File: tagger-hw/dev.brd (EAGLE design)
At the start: 65.7 x 62.2 mm, 50 parts, among them J2 22-23-2021, J3 22-23-2021, X1 EXC-31B

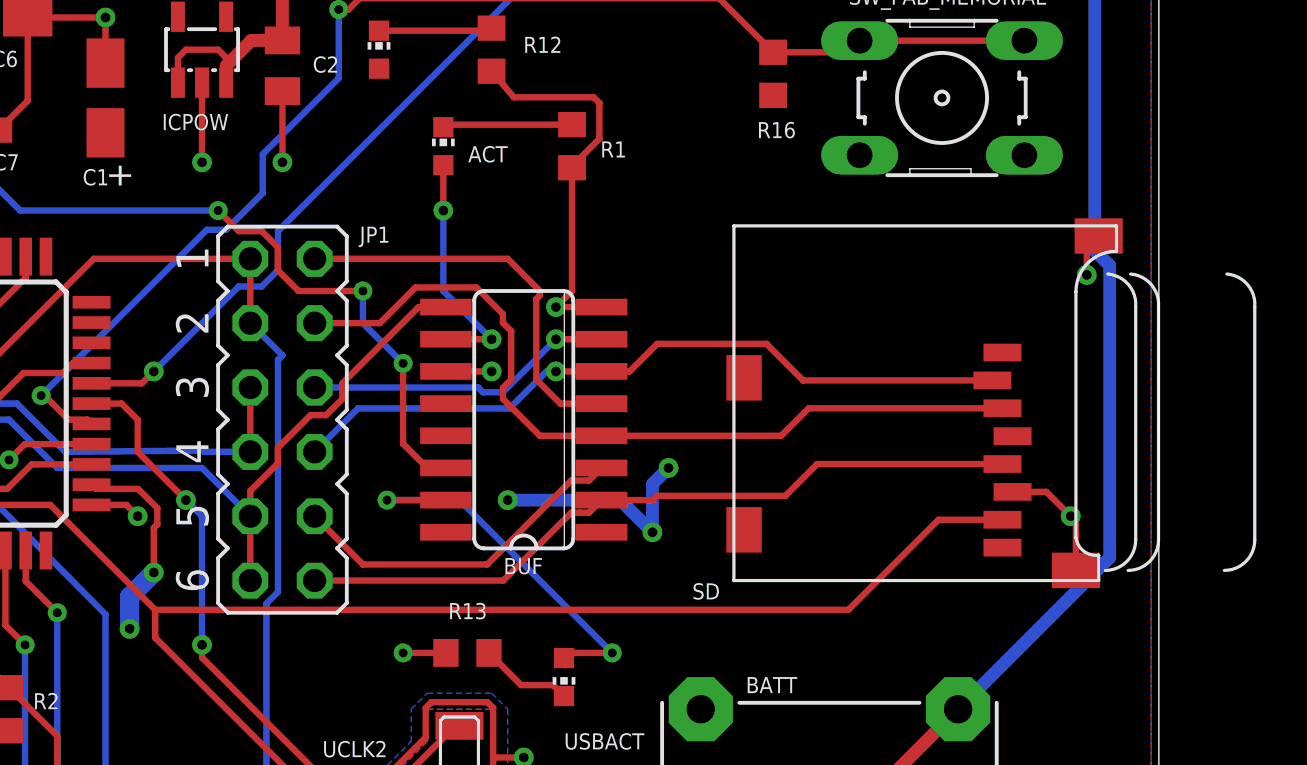
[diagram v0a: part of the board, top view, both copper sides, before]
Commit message: New microSD slot pattern
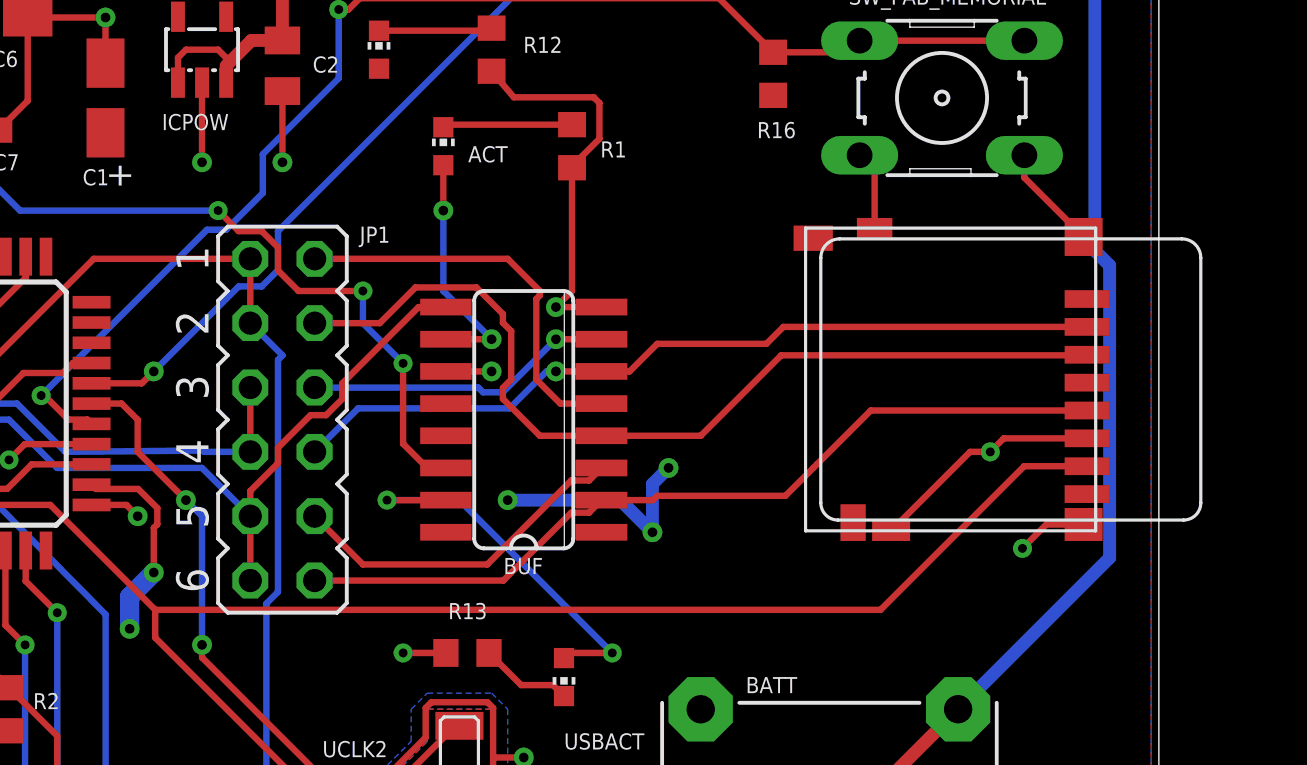
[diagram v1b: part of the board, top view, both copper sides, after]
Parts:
- removed SD: MICROSD, adafruit:MICROSD
- added U$1: MICROSD, dorskyee:MICROSD
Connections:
- net +3V3: now also U$1.VDD; no longer SD.4
- net CS_OUT: now also U$1.CS; no longer SD.2
- net GND: now also U$1.MNT@1, U$1.MNT@2, U$1.MNT@3, U$1.MNT@4, U$1.VSS; no longer SD.6, SD.MT1, SD.MT2
- net MISO: now also U$1.MISO; no longer SD.7
- net MOSI_OUT: now also U$1.MOSI; no longer SD.3
- net SCK_OUT: now also U$1.SCK; no longer SD.5
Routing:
- net GND: track 115.9 -> 128.6 mm
- net SCK_OUT: track 29.1 -> 33.3 mm
- net MOSI_OUT: track 32.8 -> 37.0 mm
- net MISO: track 71.8 -> 76.0 mm
- net CS_OUT: track 29.1 -> 32.5 mm
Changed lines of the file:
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@@
 <setting verticaltext="up"/>
 </settings>
-<grid distance="12.5" unitdist="mil" unit="mil" style="lines" multiple="1" display="no" altdistance="5" altunitdist="mil" altunit="mil"/>
+<grid distance="25" unitdist="mil" unit="mil" style="lines" multiple="2" display="no" altdistance="5" altunitdist="mil" altunit="mil"/>
 <layers>
 <layer number="1" name="Top" color="4" fill="1" visible="yes" active="yes"/>
@@
 <attribute name="VALUE" x="44.831" y="47.498" size="0.635" layer="27" font="vector" rot="R90"/>
 </element>
-<element name="SD" library="adafruit" package="MICROSD" value="MICROSD" x="48.895" y="31.115" smashed="yes" rot="R90">
-<attribute name="NAME" x="48.39" y="31.005" size="0.635" layer="25" font="vector" rot="R180"/>
-</element>
 <element name="BUF" library="40xx" library_urn="urn:adsk.eagle:library:80" package="SO16" package3d_urn="urn:adsk.eagle:package:821/2" value="4010D" x="40.64" y="37.465" smashed="yes" rot="R90">
 <attribute name="NAME" x="41.402" y="32.004" size="0.635" layer="25" font="vector" ratio="10" rot="R180"/>
@@
 <attribute name="VALUE" x="48.5775" y="51.7525" size="1.27" layer="27" rot="R270"/>
 </element>
+<element name="U$1" library="dorskyee" package="MICROSD" value="MICROSD" x="62.865" y="42.2275" rot="R90"/>
 </elements>
 <signals>
@@
 <wire x1="44.45" y1="34.29" x2="45.72" y2="33.02" width="0.508" layer="16"/>
 <via x="45.72" y="33.02" extent="1-16" drill="0.381"/>
-<contactref element="SD" pad="4"/>
 <wire x1="45.72" y1="33.02" x2="45.72" y2="34.925" width="0.508" layer="16"/>
 <wire x1="45.72" y1="34.925" x2="46.355" y2="35.56" width="0.508" layer="16"/>
@@
 <contactref element="R15" pad="2"/>
 <contactref element="R16" pad="2"/>
+<contactref element="U$1" pad="VDD"/>
 </signal>
 <signal name="GND">
@@
 <wire x1="21.06" y1="53.34" x2="21.06" y2="50.055" width="0.254" layer="1"/>
 <wire x1="21.06" y1="50.055" x2="19.9" y2="48.895" width="0.254" layer="1"/>
-<contactref element="SD" pad="6"/>
-<contactref element="SD" pad="MT2"/>
-<contactref element="SD" pad="MT1"/>
-<wire x1="62.435" y1="31.515" x2="62.435" y2="33.45" width="0.254" layer="1"/>
-<wire x1="62.435" y1="33.45" x2="62.23" y2="33.655" width="0.254" layer="1"/>
-<via x="62.23" y="33.655" extent="1-16" drill="0.381"/>
-<wire x1="62.23" y1="33.655" x2="61.27" y2="34.615" width="0.254" layer="1"/>
-<wire x1="61.27" y1="34.615" x2="59.935" y2="34.615" width="0.254" layer="1"/>
-<wire x1="63.335" y1="44.715" x2="62.865" y2="44.245" width="0.254" layer="1"/>
-<wire x1="62.865" y1="44.245" x2="62.865" y2="43.18" width="0.254" layer="1"/>
-<via x="62.865" y="43.18" extent="1-16" drill="0.381"/>
 <contactref element="UCLK2" pad="P$4"/>
 <contactref element="C9" pad="2"/>
@@
 <contactref element="SW_FAB_MEMORIAL" pad="4"/>
 <contactref element="SW_FAB_MEMORIAL" pad="3"/>
+<contactref element="U$1" pad="VSS"/>
+<wire x1="62.865" y1="36.7275" x2="59.5875" y2="36.7275" width="0.254" layer="1"/>
+<wire x1="59.5875" y1="36.7275" x2="59.055" y2="36.195" width="0.254" layer="1"/>
+<via x="59.055" y="36.195" extent="1-16" drill="0.35"/>
+<contactref element="U$1" pad="MNT@4"/>
+<contactref element="U$1" pad="MNT@3"/>
+<contactref element="U$1" pad="MNT@2"/>
+<contactref element="U$1" pad="MNT@1"/>
+<wire x1="55.14" y1="33.0775" x2="58.2575" y2="36.195" width="0.254" layer="1"/>
+<wire x1="58.2575" y1="36.195" x2="59.055" y2="36.195" width="0.254" layer="1"/>
+<wire x1="62.74" y1="44.6775" x2="60.4012" y2="47.0163" width="0.254" layer="1"/>
+<wire x1="60.4012" y1="47.0163" x2="60.4012" y2="47.9044" width="0.254" layer="1"/>
+<wire x1="54.49" y1="45.0275" x2="54.49" y2="47.3132" width="0.254" layer="1"/>
+<wire x1="54.49" y1="47.3132" x2="53.8988" y2="47.9044" width="0.254" layer="1"/>
+<wire x1="62.74" y1="33.3275" x2="61.2675" y2="33.3275" width="0.254" layer="1"/>
+<wire x1="61.2675" y1="33.3275" x2="60.325" y2="32.385" width="0.254" layer="1"/>
+<via x="60.325" y="32.385" extent="1-16" drill="0.35"/>
 </signal>
 <signal name="VCC">
@@
 </signal>
 <signal name="MISO">
-<contactref element="SD" pad="7"/>
 <contactref element="UC" pad="11"/>
 <contactref element="ISP1" pad="1"/>
 <wire x1="11.98" y1="34.1" x2="21.95138125" y2="34.1" width="0.254" layer="1"/>
-<wire x1="53.4543" y1="29.9593" x2="57.01" y2="33.515" width="0.254" layer="1"/>
-<wire x1="59.535" y1="33.515" x2="57.01" y2="33.515" width="0.254" layer="1"/>
 <wire x1="10.85809375" y1="34.1" x2="11.98" y2="34.1" width="0.254" layer="1"/>
 <wire x1="8.14079375" y1="36.8173" x2="10.85809375" y2="34.1" width="0.254" layer="1"/>
@@
 <wire x1="7.12460625" y1="36.8173" x2="8.14079375" y2="36.8173" width="0.254" layer="1"/>
 <wire x1="6.3627" y1="37.57920625" x2="7.12460625" y2="36.8173" width="0.254" layer="1"/>
-<wire x1="26.09208125" y1="29.9593" x2="53.4543" y2="29.9593" width="0.254" layer="1"/>
+<wire x1="26.09208125" y1="29.9593" x2="54.7243" y2="29.9593" width="0.254" layer="1"/>
 <wire x1="21.95138125" y1="34.1" x2="26.09208125" y2="29.9593" width="0.254" layer="1"/>
 <contactref element="UCLK2" pad="P$2"/>
@@
 <wire x1="32.3071875" y1="22.644" x2="26.09208125" y2="28.85910625" width="0.254" layer="1"/>
 <wire x1="26.09208125" y1="28.85910625" x2="26.09208125" y2="29.9593" width="0.254" layer="1"/>
+<contactref element="U$1" pad="MISO"/>
+<wire x1="60.3925" y1="35.6275" x2="62.865" y2="35.6275" width="0.254" layer="1"/>
+<wire x1="54.7243" y1="29.9593" x2="60.3925" y2="35.6275" width="0.254" layer="1"/>
 </signal>
 <signal name="SD_ACT_D">
@@
 </signal>
 <signal name="MOSI_OUT">
-<contactref element="SD" pad="3"/>
 <contactref element="JP1" pad="4"/>
 <contactref element="BUF" pad="4"/>
-<wire x1="51.885" y1="37.915" x2="59.535" y2="37.915" width="0.254" layer="1"/>
-<wire x1="43.7134" y1="36.83" x2="50.8" y2="36.83" width="0.254" layer="1"/>
-<wire x1="50.8" y1="36.83" x2="51.885" y2="37.915" width="0.254" layer="1"/>
 <wire x1="36.36648125" y1="42.6847" x2="38.76671875" y2="42.6847" width="0.254" layer="1"/>
 <wire x1="32.385" y1="41.275" x2="34.95678125" y2="41.275" width="0.254" layer="1"/>
@@
 <wire x1="39.8173" y1="38.72170625" x2="39.8173" y2="38.2877" width="0.254" layer="1"/>
 <wire x1="40.1447" y1="40.96089375" x2="40.1447" y2="39.04910625" width="0.254" layer="1"/>
+<contactref element="U$1" pad="MOSI"/>
+<wire x1="62.865" y1="40.0275" x2="62.8425" y2="40.005" width="0.254" layer="1"/>
+<wire x1="62.8425" y1="40.005" x2="50.8" y2="40.005" width="0.254" layer="1"/>
+<wire x1="47.625" y1="36.83" x2="43.7134" y2="36.83" width="0.254" layer="1"/>
+<wire x1="50.8" y1="40.005" x2="47.625" y2="36.83" width="0.254" layer="1"/>
 </signal>
 <signal name="SCK_OUT">
-<contactref element="SD" pad="5"/>
 <contactref element="BUF" pad="2"/>
 <wire x1="43.7134" y1="34.29" x2="45.74138125" y2="34.29" width="0.254" layer="1"/>
-<wire x1="59.535" y1="35.715" x2="52.225" y2="35.715" width="0.254" layer="1"/>
-<wire x1="50.9695" y1="34.4595" x2="52.225" y2="35.715" width="0.254" layer="1"/>
+<wire x1="50.9695" y1="34.4595" x2="52.07" y2="35.56" width="0.254" layer="1"/>
 <contactref element="JP1" pad="12"/>
+<wire x1="52.07" y1="35.56" x2="52.225" y2="35.715" width="0.254" layer="1"/>
 <wire x1="43.7134" y1="34.29" x2="43.2181" y2="33.7947" width="0.254" layer="1"/>
-<wire x1="43.2181" y1="33.7947" x2="42.8625" y2="33.7947" width="0.254" layer="1"/>
-<wire x1="42.8625" y1="33.7947" x2="42.51328125" y2="33.7947" width="0.254" layer="1"/>
+<wire x1="43.2181" y1="33.7947" x2="42.51328125" y2="33.7947" width="0.254" layer="1"/>
 <wire x1="39.83358125" y1="31.115" x2="32.385" y2="31.115" width="0.254" layer="1"/>
 <wire x1="42.51328125" y1="33.7947" x2="39.83358125" y2="31.115" width="0.254" layer="1"/>
 <wire x1="45.74138125" y1="34.29" x2="45.91088125" y2="34.4595" width="0.254" layer="1"/>
 <wire x1="45.91088125" y1="34.4595" x2="50.9695" y2="34.4595" width="0.254" layer="1"/>
+<contactref element="U$1" pad="SCK"/>
+<wire x1="62.865" y1="37.8275" x2="54.3375" y2="37.8275" width="0.254" layer="1"/>
+<wire x1="54.3375" y1="37.8275" x2="52.225" y2="35.715" width="0.254" layer="1"/>
 </signal>
 <signal name="CS_OUT">
-<contactref element="SD" pad="2"/>
 <contactref element="BUF" pad="6"/>
 <wire x1="43.7134" y1="39.37" x2="44.82138125" y2="39.37" width="0.254" layer="1"/>
-<wire x1="51.66361875" y1="39.015" x2="50.21911875" y2="40.4595" width="0.254" layer="1"/>
-<wire x1="59.135" y1="39.015" x2="51.66361875" y2="39.015" width="0.254" layer="1"/>
 <contactref element="JP1" pad="8"/>
 <wire x1="43.7134" y1="39.37" x2="41.91" y2="39.37" width="0.254" layer="1"/>
@@
 <wire x1="44.82138125" y1="39.37" x2="45.91088125" y2="40.4595" width="0.254" layer="1"/>
 <wire x1="45.91088125" y1="40.4595" x2="50.21911875" y2="40.4595" width="0.254" layer="1"/>
+<contactref element="U$1" pad="CS"/>
+<wire x1="62.865" y1="41.1275" x2="50.88711875" y2="41.1275" width="0.254" layer="1"/>
+<wire x1="50.88711875" y1="41.1275" x2="50.21911875" y2="40.4595" width="0.254" layer="1"/>
 </signal>
 <signal name="VBAT">

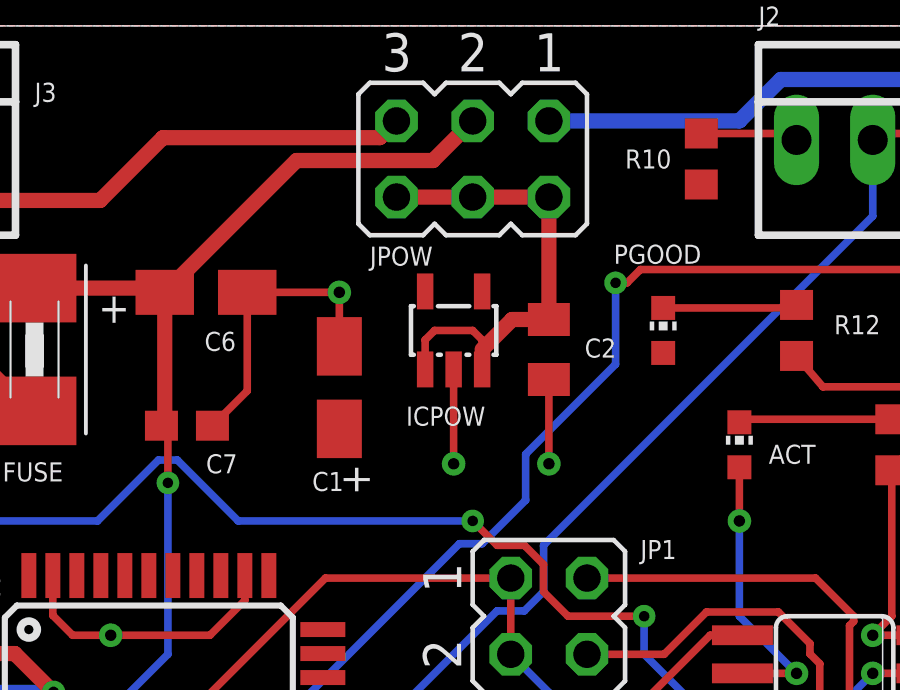
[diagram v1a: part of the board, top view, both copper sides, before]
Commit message: Add current sense resistor, calculations
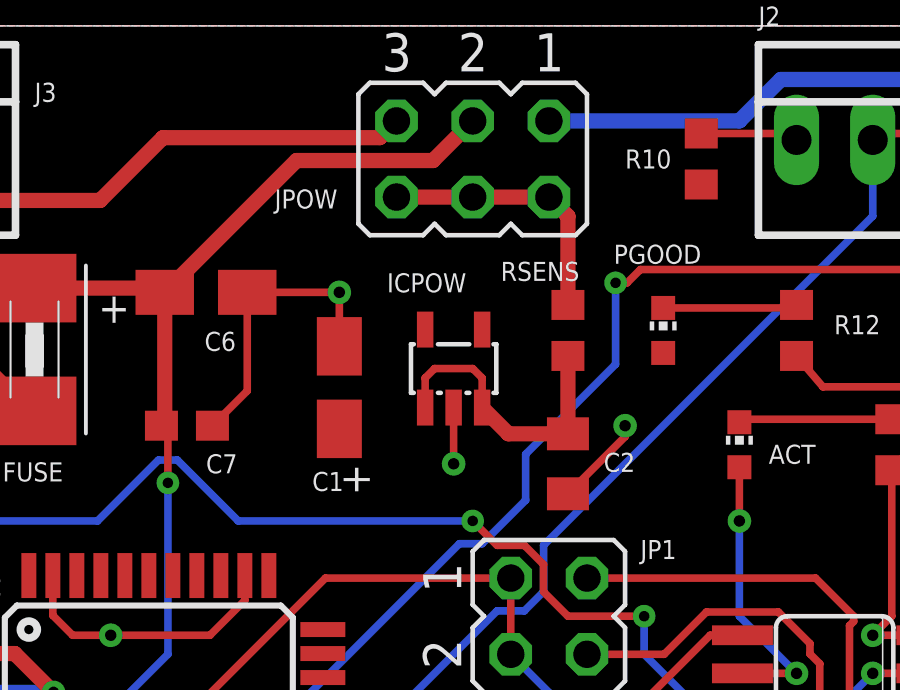
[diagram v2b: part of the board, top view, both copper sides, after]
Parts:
- added RSENS: 1R, adafruit:R0603
- moved C2 3.86 mm to (31.8, 47.6)
- moved ICPOW 1.27 mm to (27.9, 50.8)
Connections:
- new net VCC_R: C2.1, ICPOW.1, ICPOW.3, RSENS.1
- net VCC: now also RSENS.2; no longer C2.1, ICPOW.1, ICPOW.3
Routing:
- net VCC_R: track 0.00 -> 9.95 mm
- net VCC: track 15.9 -> 8.94 mm
- net GND: track 128.6 -> 127.6 mm
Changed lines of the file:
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@@
 <attribute name="VALUE" x="21.805" y="52.115" size="0.635" layer="27" font="vector" rot="R270"/>
 </element>
-<element name="C2" library="adafruit" package="C0805K" value="0.1uF" x="31.115" y="51.435" smashed="yes" rot="R270">
-<attribute name="NAME" x="32.3075" y="51.165" size="0.635" layer="25" font="vector"/>
-<attribute name="VALUE" x="29.215" y="52.435" size="0.635" layer="27" font="vector" rot="R270"/>
-</element>
-<element name="ICPOW" library="adafruit" package="SOT23-5L" value="CAT6219-330TDGT3" x="27.94" y="52.07" smashed="yes">
-<attribute name="NAME" x="26.3525" y="48.895" size="0.635" layer="25" font="vector"/>
-<attribute name="VALUE" x="26.035" y="48.641" size="0.635" layer="27" font="vector"/>
+<element name="C2" library="adafruit" package="C0805K" value="0.1uF" x="31.75" y="47.625" smashed="yes" rot="R270">
+<attribute name="NAME" x="32.9425" y="47.355" size="0.635" layer="25" font="vector"/>
+<attribute name="VALUE" x="29.85" y="48.625" size="0.635" layer="27" font="vector" rot="R270"/>
+</element>
+<element name="ICPOW" library="adafruit" package="SOT23-5L" value="CAT6219-330TDGT3" x="27.94" y="50.8" smashed="yes">
+<attribute name="NAME" x="25.7175" y="53.34" size="0.635" layer="25" font="vector"/>
+<attribute name="VALUE" x="26.035" y="47.371" size="0.635" layer="27" font="vector"/>
 </element>
 <element name="R1" library="adafruit" package="R0603" value="1K" x="42.545" y="48.26" smashed="yes" rot="R90">
@@
 </element>
 <element name="JPOW" library="jumper" library_urn="urn:adsk.eagle:library:252" package="JP3Q" package3d_urn="urn:adsk.eagle:package:15460/1" value="HDR100IMP40M-G-V-TH" x="28.575" y="57.785" smashed="yes" rot="R180">
-<attribute name="NAME" x="27.2415" y="54.864" size="0.635" layer="25" font="vector" ratio="10" rot="R180"/>
+<attribute name="NAME" x="24.0665" y="56.769" size="0.635" layer="25" font="vector" ratio="10" rot="R180"/>
 <attribute name="VALUE" x="32.004" y="63.627" size="0.635" layer="27" font="vector" ratio="10" rot="R180"/>
 </element>
@@
 </element>
 <element name="U$1" library="dorskyee" package="MICROSD" value="MICROSD" x="62.865" y="42.2275" rot="R90"/>
+<element name="RSENS" library="adafruit" package="R0603" value="1R" x="31.75" y="52.07" smashed="yes" rot="R90">
+<attribute name="NAME" x="32.131" y="54.356" size="0.635" layer="25" font="vector" rot="R180"/>
+<attribute name="VALUE" x="33.782" y="51.181" size="1.27" layer="27" rot="R90"/>
+</element>
 </elements>
 <signals>
@@
 <wire x1="24.955" y1="34.1" x2="25.4" y2="33.655" width="0.254" layer="1"/>
 <via x="25.4" y="33.655" extent="1-16" drill="0.381"/>
-<wire x1="27.94" y1="50.77" x2="27.94" y2="47.625" width="0.254" layer="1"/>
+<wire x1="27.94" y1="49.5" x2="27.94" y2="47.625" width="0.254" layer="1"/>
 <via x="27.94" y="47.625" extent="1-16" drill="0.381"/>
 <wire x1="24.13" y1="51.54" x2="24.13" y2="53.34" width="0.254" layer="1"/>
 <via x="24.13" y="53.34" extent="1-16" drill="0.381"/>
-<wire x1="31.115" y1="50.435" x2="31.115" y2="47.625" width="0.254" layer="1"/>
-<via x="31.115" y="47.625" extent="1-16" drill="0.381"/>
+<via x="33.655" y="48.895" extent="1-16" drill="0.381"/>
 <wire x1="29.77" y1="8.89" x2="31.75" y2="8.89" width="0.254" layer="1"/>
 <via x="31.75" y="8.89" extent="1-16" drill="0.381"/>
@@
 <wire x1="61.2675" y1="33.3275" x2="60.325" y2="32.385" width="0.254" layer="1"/>
 <via x="60.325" y="32.385" extent="1-16" drill="0.35"/>
+<wire x1="31.75" y1="46.625" x2="33.655" y2="48.53" width="0.254" layer="1"/>
+<wire x1="33.655" y1="48.53" x2="33.655" y2="48.895" width="0.254" layer="1"/>
 </signal>
 <signal name="VCC">
-<contactref element="ICPOW" pad="1"/>
-<contactref element="C2" pad="1"/>
-<contactref element="ICPOW" pad="3"/>
 <contactref element="JPOW" pad="2"/>
 <contactref element="JPOW" pad="6"/>
@@
 <wire x1="26.035" y1="56.515" x2="28.575" y2="56.515" width="0.508" layer="1"/>
 <wire x1="28.575" y1="56.515" x2="31.115" y2="56.515" width="0.508" layer="1"/>
-<wire x1="31.115" y1="52.435" x2="31.115" y2="56.515" width="0.508" layer="1"/>
-<wire x1="26.99" y1="50.77" x2="26.99" y2="51.755" width="0.254" layer="1"/>
-<wire x1="26.99" y1="51.755" x2="27.305" y2="52.07" width="0.254" layer="1"/>
-<wire x1="27.305" y1="52.07" x2="28.575" y2="52.07" width="0.254" layer="1"/>
-<wire x1="28.89" y1="51.755" x2="28.575" y2="52.07" width="0.254" layer="1"/>
-<wire x1="28.89" y1="50.77" x2="28.89" y2="51.435" width="0.254" layer="1"/>
-<wire x1="28.89" y1="51.435" x2="28.89" y2="51.755" width="0.254" layer="1"/>
-<wire x1="31.115" y1="52.435" x2="29.89" y2="52.435" width="0.508" layer="1"/>
-<wire x1="29.89" y1="52.435" x2="28.89" y2="51.435" width="0.508" layer="1"/>
+<wire x1="31.115" y1="56.515" x2="31.75" y2="55.88" width="0.508" layer="1"/>
+<contactref element="RSENS" pad="2"/>
+<wire x1="31.75" y1="55.88" x2="31.75" y2="52.92" width="0.508" layer="1"/>
 </signal>
 <signal name="MISO">
@@
 <wire x1="26.3236875" y1="5.6125" x2="29.21" y2="5.6125" width="0.254" layer="1"/>
 </signal>
+<signal name="VCC_R">
+<contactref element="ICPOW" pad="1"/>
+<contactref element="ICPOW" pad="3"/>
+<wire x1="26.99" y1="49.5" x2="26.99" y2="50.485" width="0.254" layer="1"/>
+<wire x1="26.99" y1="50.485" x2="27.305" y2="50.8" width="0.254" layer="1"/>
+<wire x1="27.305" y1="50.8" x2="28.575" y2="50.8" width="0.254" layer="1"/>
+<wire x1="28.89" y1="50.485" x2="28.575" y2="50.8" width="0.254" layer="1"/>
+<wire x1="28.89" y1="49.5" x2="28.89" y2="50.485" width="0.254" layer="1"/>
+<contactref element="RSENS" pad="1"/>
+<contactref element="C2" pad="1"/>
+<wire x1="29.765" y1="48.625" x2="28.89" y2="49.5" width="0.508" layer="1"/>
+<wire x1="31.75" y1="51.22" x2="31.75" y2="48.625" width="0.508" layer="1"/>
+<wire x1="31.75" y1="48.625" x2="29.765" y2="48.625" width="0.508" layer="1"/>
+</signal>
 </signals>
